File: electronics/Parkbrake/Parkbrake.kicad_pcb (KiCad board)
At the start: 2 copper layers, 101.6 x 114.3 mm, 353 parts, among them P1 Conn48pin, P2 JTAG, P3 UART, Q1 BSS138, Q10 IPD031N06L3 G, Q11 IPD031N06L3 G, Q12 NX3008CBKS, Q13 NX3008CBKS, Q14 IPD031N06L3 G, Q15 IPD031N06L3 G, Q16 IPD031N06L3 G, Q17 IPD031N06L3 G, Q18 NX3008CBKS, Q19 NX3008CBKS, Q2 BSS138, Q20 IPD031N06L3 G, Q21 IPD031N06L3 G, Q22 IPD031N06L3 G, Q23 IPD031N06L3 G, Q24 NX3008CBKS, Q25 NX3008CBKS, Q26 IPD031N06L3 G, Q27 IPD031N06L3 G, Q28 IPD031N06L3 G, Q29 IPD031N06L3 G, Q3 P-ch -40V 0.0035ohm, Q30 NX3008CBKS, Q31 BSS138, Q32 NTS4173, Q33 NX3008CBKS, Q4 P-ch -40V 0.0035ohm, Q5 BSS308, Q6 BSS308, Q7 NX3008CBKS, Q8 IPD031N06L3 G, Q9 IPD031N06L3 G, U1 74LVC00, U10 IRS2304, U11 ZXCT1082, U12 IRS2304, U13 LM2903, U14 IRS2304, U15 ZXCT1082, U16 IRS2304, U17 LM2903, U18 IRS2304, U19 ZXCT1082, U2 74LVC08, U20 IRS2304, U21 MIC2619, U22 MC34063, U23 LD1117S33CTR, U24 CAT25160_EEPROM, U25 STM32F373RBTx, U26 SN65HVD1050D, U27 SN74LVC245ADBR, U28 SN74HC20, U29 SN74HC02, U3 74LVC00, U30 SN74HC132, U31 MAX232, U32 MAX232, U33 NCV1124, U34 NCV1124, U35 74LVC08, U4 74LVC08, U5 LM2903, U6 IRS2304, U7 ZXCT1082, U8 IRS2304, U9 LM2903, Y1 24Mhz

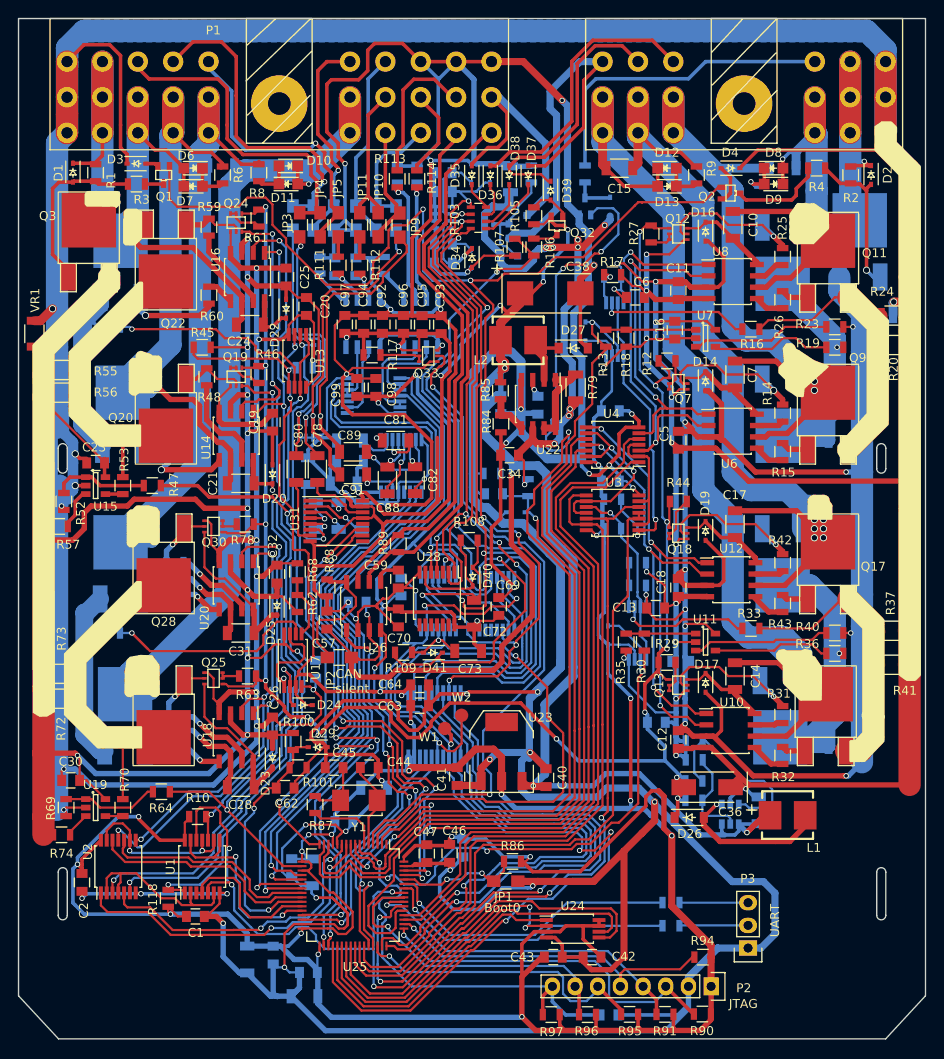
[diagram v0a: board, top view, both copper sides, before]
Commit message: Added copperareas
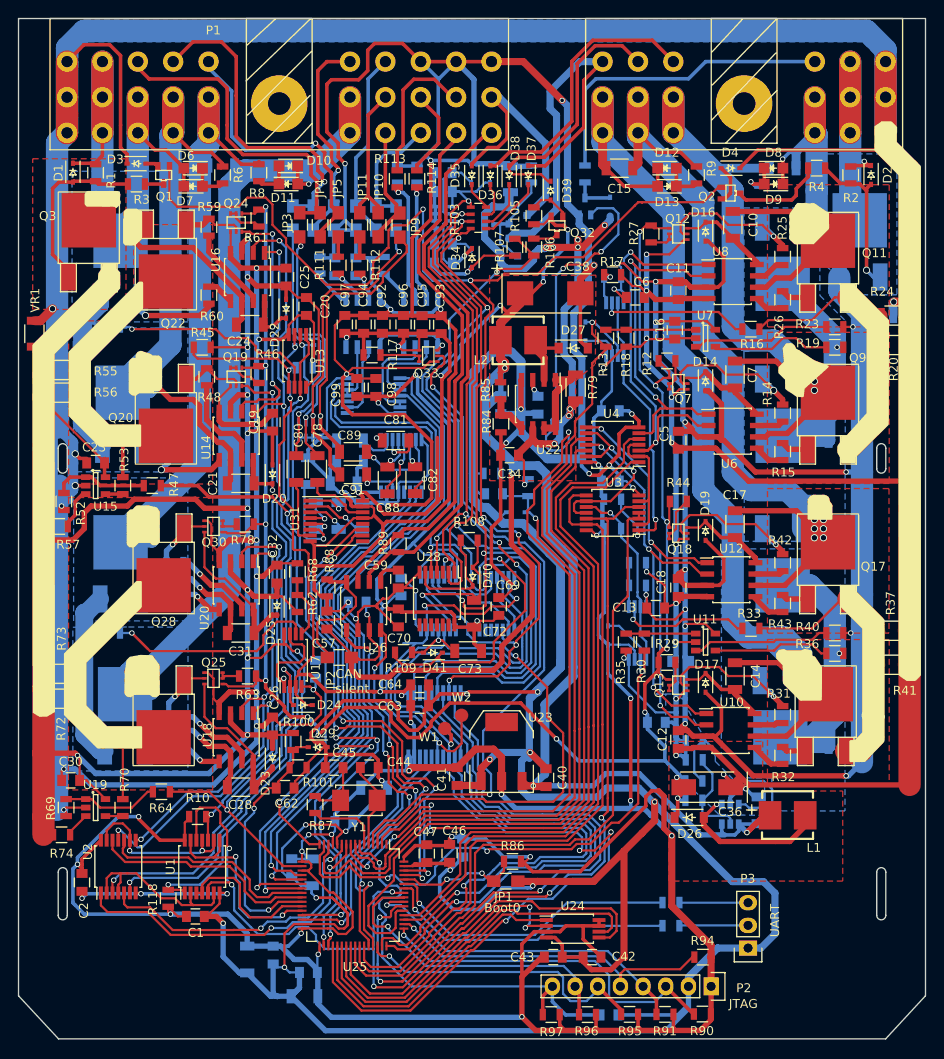
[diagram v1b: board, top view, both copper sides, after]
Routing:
- net GNDPWR: track 748.7 -> 754.2 mm, vias 30 -> 31
- added copper zone on F.Cu, net /+12V_BatF
- added copper zone on B.Cu, net /+12V_BatR
- added copper zone on F.Cu, net GNDPWR
- added copper zone on F.Cu, net LR_wheelsensor_in-
- added copper zone on B.Cu, net LeftFrontMotor+
- added copper zone on B.Cu, net LeftFrontMotor-
- added copper zone on F.Cu, net LeftRearMotor+
- added copper zone on F.Cu, net LeftRearMotor-
- added copper zone on B.Cu, net Net-(Q10-Pad2)
- added copper zone on B.Cu, net Net-(Q14-Pad2)
- added copper zone on F.Cu, net Net-(Q20-Pad2)
- added copper zone on F.Cu, net Net-(Q26-Pad2)
- added copper zone on B.Cu, net RightFrontMotor+
- added copper zone on B.Cu, net RightFrontMotor-
- added copper zone on F.Cu, net RightRearMotor+
- added copper zone on F.Cu, net RightRearMotor-
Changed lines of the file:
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@@
     (thickness 1.6)
     (drawings 87)
-    (tracks 6120)
+    (tracks 6125)
     (zones 0)
     (modules 353)
@@
     (34 B.Paste user)
     (35 F.Paste user)
-    (36 B.SilkS user hide)
+    (36 B.SilkS user)
     (37 F.SilkS user)
     (38 B.Mask user)
@@
   )
   (setup
-    (last_trace_width 1.2)
+    (last_trace_width 0.4)
     (user_trace_width 0.4)
     (user_trace_width 0.6)
@@
   (segment (start 131.15544 59.2099) (end 129.518 59.2099) (width 0.8) (layer B.Cu) (net 3))
   (segment (start 129.518 59.2099) (end 129.3749 59.0668) (width 0.8) (layer B.Cu) (net 3))
+  (segment (start 155.9306 126.1413) (end 155.9306 123.5202) (width 0.4) (layer B.Cu) (net 4))
+  (segment (start 155.9306 123.5202) (end 155.1813 122.7709) (width 0.4) (layer B.Cu) (net 4))
+  (via (at 155.1813 122.7709) (size 0.6) (drill 0.4) (layers F.Cu B.Cu) (net 4))
+  (segment (start 155.1813 122.7709) (end 155.96362 123.55322) (width 0.4) (layer F.Cu) (net 4))
+  (segment (start 155.96362 123.55322) (end 155.96362 124.206) (width 0.4) (layer F.Cu) (net 4))
   (segment (start 80.391 81.153) (end 80.391 84.3153) (width 1.2) (layer B.Cu) (net 4))
   (segment (start 80.391 84.3153) (end 80.6577 84.582) (width 1.2) (layer B.Cu) (net 4))
@@
     (connect_pads (clearance 0.508))
     (min_thickness 0.254)
-    (fill (arc_segments 16) (thermal_gap 0.508) (thermal_bridge_width 0.508))
+    (fill yes (arc_segments 16) (thermal_gap 0.508) (thermal_bridge_width 0.508))
     (polygon
       (pts
@@
     (connect_pads (clearance 0.508))
     (min_thickness 0.254)
-    (fill (arc_segments 16) (thermal_gap 0.508) (thermal_bridge_width 0.508))
+    (fill yes (arc_segments 16) (thermal_gap 0.508) (thermal_bridge_width 0.508))
     (polygon
       (pts
@@
       )
     )
+  )
+  (zone (net 17) (net_name LeftFrontMotor-) (layer B.Cu) (hatch edge 0.508)
+    (connect_pads yes (clearance 0.508))
+    (min_thickness 0.254)
+    (fill yes (arc_segments 16) (thermal_gap 0.508) (thermal_bridge_width 0.508))
+    (polygon
+      (pts
+        (xy 95.1738 55.1688) (xy 95.1738 72.0852) (xy 82.1944 72.0852) (xy 82.1944 55.2069) (xy 91.5924 55.2069)
+      )
+    )
+  )
+  (zone (net 15) (net_name LeftFrontMotor+) (layer B.Cu) (hatch edge 0.508)
+    (connect_pads yes (clearance 0.508))
+    (min_thickness 0.254)
+    (fill yes (arc_segments 16) (thermal_gap 0.508) (thermal_bridge_width 0.508))
+    (polygon
+      (pts
+        (xy 93.40215 72.771) (xy 95.1738 72.771) (xy 95.171024 72.78359) (xy 95.1865 72.7837) (xy 95.171003 72.783685)
+        (xy 95.1611 88.9) (xy 82.3595 88.8746) (xy 82.3341 72.771) (xy 91.6178 72.771) (xy 91.6178 72.7583)
+        (xy 93.40215 72.771)
+      )
+    )
+  )
+  (zone (net 21) (net_name RightFrontMotor-) (layer B.Cu) (hatch edge 0.508)
+    (connect_pads yes (clearance 0.508))
+    (min_thickness 0.254)
+    (fill yes (arc_segments 16) (thermal_gap 0.508) (thermal_bridge_width 0.508))
+    (polygon
+      (pts
+        (xy 95.1611 89.5604) (xy 95.1738 105.5751) (xy 82.3722 105.5878) (xy 82.3722 89.5731) (xy 82.3595 89.5604)
+      )
+    )
+  )
+  (zone (net 19) (net_name RightFrontMotor+) (layer B.Cu) (hatch edge 0.508)
+    (connect_pads yes (clearance 0.508))
+    (min_thickness 0.254)
+    (fill yes (arc_segments 16) (thermal_gap 0.508) (thermal_bridge_width 0.508))
+    (polygon
+      (pts
+        (xy 95.1865 106.2863) (xy 95.1738 122.3772) (xy 82.2833 122.3899) (xy 82.2833 106.2863) (xy 88.5063 106.2609)
+      )
+    )
+  )
+  (zone (net 197) (net_name /+12V_BatR) (layer B.Cu) (hatch edge 0.508)
+    (connect_pads yes (clearance 0.508))
+    (min_thickness 0.254)
+    (fill yes (arc_segments 16) (thermal_gap 0.508) (thermal_bridge_width 0.508))
+    (polygon
+      (pts
+        (xy 166.878 53.2638) (xy 174.5996 53.2638) (xy 174.5996 69.0499) (xy 170.4086 69.0499) (xy 166.5224 65.6971)
+        (xy 166.5224 53.2638) (xy 166.8399 53.2638)
+      )
+    )
+  )
+  (zone (net 101) (net_name "Net-(Q10-Pad2)") (layer B.Cu) (hatch edge 0.508)
+    (connect_pads yes (clearance 0.508))
+    (min_thickness 0.254)
+    (fill yes (arc_segments 16) (thermal_gap 0.508) (thermal_bridge_width 0.508))
+    (polygon
+      (pts
+        (xy 157.4673 59.3217) (xy 165.9763 59.3217) (xy 165.9636 69.1261) (xy 168.8338 71.9582) (xy 168.783 96.6597)
+        (xy 157.5054 96.6597) (xy 157.4673 75.7682) (xy 157.4673 64.5795)
+      )
+    )
+  )
+  (zone (net 214) (net_name "Net-(Q14-Pad2)") (layer B.Cu) (hatch edge 0.508)
+    (connect_pads yes (clearance 0.508))
+    (min_thickness 0.254)
+    (fill yes (arc_segments 16) (thermal_gap 0.508) (thermal_bridge_width 0.508))
+    (polygon
+      (pts
+        (xy 168.783 97.536) (xy 168.783 126.873) (xy 160.5788 126.8603) (xy 160.5788 123.2027) (xy 157.099 123.1392)
+        (xy 154.9273 120.9421) (xy 154.9527 97.5106) (xy 168.783 97.5106) (xy 168.783 97.536)
+      )
+    )
+  )
+  (zone (net 8) (net_name LeftRearMotor-) (layer F.Cu) (hatch edge 0.508)
+    (connect_pads yes (clearance 0.508))
+    (min_thickness 0.254)
+    (fill yes (arc_segments 16) (thermal_gap 0.508) (thermal_bridge_width 0.508))
+    (polygon
+      (pts
+        (xy 160.0962 56.7182) (xy 173.736 56.7182) (xy 173.736 72.644) (xy 160.0962 72.644) (xy 160.0962 57.3405)
+      )
+    )
+  )
+  (zone (net 6) (net_name LeftRearMotor+) (layer F.Cu) (hatch edge 0.508)
+    (connect_pads yes (clearance 0.508))
+    (min_thickness 0.254)
+    (fill yes (arc_segments 16) (thermal_gap 0.508) (thermal_bridge_width 0.508))
+    (polygon
+      (pts
+        (xy 160.0835 73.2536) (xy 173.736 73.2536) (xy 173.736 90.1827) (xy 160.0962 90.1827) (xy 160.0962 83.7438)
+      )
+    )
+  )
+  (zone (net 12) (net_name RightRearMotor-) (layer F.Cu) (hatch edge 0.508)
+    (connect_pads yes (clearance 0.508))
+    (min_thickness 0.254)
+    (fill yes (arc_segments 16) (thermal_gap 0.508) (thermal_bridge_width 0.508))
+    (polygon
+      (pts
+        (xy 160.0962 90.7542) (xy 173.7106 90.7542) (xy 173.7106 106.9467) (xy 160.0962 106.9467) (xy 160.0962 100.3173)
+      )
+    )
+  )
+  (zone (net 10) (net_name RightRearMotor+) (layer F.Cu) (hatch edge 0.508)
+    (connect_pads yes (clearance 0.508))
+    (min_thickness 0.254)
+    (fill yes (arc_segments 16) (thermal_gap 0.508) (thermal_bridge_width 0.508))
+    (polygon
+      (pts
+        (xy 160.0962 107.6706) (xy 173.736 107.6706) (xy 173.736 123.8758) (xy 160.0962 123.8758) (xy 160.0962 111.1377)
+      )
+    )
+  )
+  (zone (net 196) (net_name /+12V_BatF) (layer F.Cu) (hatch edge 0.508)
+    (connect_pads yes (clearance 0.508))
+    (min_thickness 0.254)
+    (fill yes (arc_segments 16) (thermal_gap 0.508) (thermal_bridge_width 0.508))
+    (polygon
+      (pts
+        (xy 77.7875 53.8099) (xy 88.2396 53.8099) (xy 88.2396 70.6882) (xy 77.7875 70.6882) (xy 77.7875 57.5056)
+      )
+    )
+  )
+  (zone (net 218) (net_name "Net-(Q20-Pad2)") (layer F.Cu) (hatch edge 0.508)
+    (connect_pads yes (clearance 0.508))
+    (min_thickness 0.254)
+    (fill yes (arc_segments 16) (thermal_gap 0.508) (thermal_bridge_width 0.508))
+    (polygon
+      (pts
+        (xy 97.9551 90.2462) (xy 81.8134 90.2462) (xy 81.8134 71.9709) (xy 88.1126 71.9709) (xy 89.1286 71.0946)
+        (xy 89.0778 61.1886) (xy 97.9551 61.1886) (xy 97.9551 90.2462)
+      )
+    )
+  )
+  (zone (net 218) (net_name "Net-(Q20-Pad2)") (layer F.Cu) (hatch edge 0.508)
+    (connect_pads yes (clearance 0.508))
+    (min_thickness 0.254)
+    (fill yes (arc_segments 16) (thermal_gap 0.508) (thermal_bridge_width 0.508))
+    (polygon
+      (pts
+        (xy 97.9678 61.1886) (xy 97.9678 61.2013) (xy 97.9551 61.1886) (xy 97.9678 61.1886)
+      )
+    )
+  )
+  (zone (net 222) (net_name "Net-(Q26-Pad2)") (layer F.Cu) (hatch edge 0.508)
+    (connect_pads yes (clearance 0.508))
+    (min_thickness 0.254)
+    (fill yes (arc_segments 16) (thermal_gap 0.508) (thermal_bridge_width 0.508))
+    (polygon
+      (pts
+        (xy 97.9551 91.7575) (xy 97.9551 124.5108) (xy 81.788 124.5108) (xy 81.788 113.9698) (xy 81.813328 91.7575)
+        (xy 97.9551 91.7575)
+      )
+    )
+  )
+  (zone (net 222) (net_name "Net-(Q26-Pad2)") (layer F.Cu) (hatch edge 0.508)
+    (connect_pads yes (clearance 0.508))
+    (min_thickness 0.254)
+    (fill yes (arc_segments 16) (thermal_gap 0.508) (thermal_bridge_width 0.508))
+    (polygon
+      (pts
+        (xy 81.7499 91.7575) (xy 81.8134 91.694) (xy 81.813328 91.7575) (xy 81.7499 91.7575)
+      )
+    )
+  )
+  (zone (net 2) (net_name LR_wheelsensor_in-) (layer F.Cu) (hatch edge 0.508)
+    (connect_pads (clearance 0.508))
+    (min_thickness 0.254)
+    (fill yes (arc_segments 16) (thermal_gap 0.508) (thermal_bridge_width 0.508))
+    (polygon
+      (pts
+        (xy 128.9812 76.7334) (xy 128.9812 89.8779) (xy 138.6332 89.8779) (xy 138.6078 78.6638) (xy 140.8176 76.8096)
+        (xy 140.8811 66.8528) (xy 128.9685 66.8909) (xy 128.9685 67.1703)
+      )
+    )
+  )
+  (zone (net 4) (net_name GNDPWR) (layer F.Cu) (hatch edge 0.508)
+    (connect_pads (clearance 0.508))
+    (min_thickness 0.254)
+    (fill yes (arc_segments 16) (thermal_gap 0.508) (thermal_bridge_width 0.508))
+    (polygon
+      (pts
+        (xy 149.0599 119.0752) (xy 159.5628 119.0752) (xy 159.5628 124.6378) (xy 168.529 124.6378) (xy 168.529 134.7216)
+        (xy 149.0472 134.7216) (xy 149.0472 132.0927)
+      )
+    )
+  )
+  (zone (net 4) (net_name GNDPWR) (layer B.Cu) (hatch edge 0.508)
+    (connect_pads (clearance 0.508))
+    (min_thickness 0.254)
+    (fill yes (arc_segments 16) (thermal_gap 0.508) (thermal_bridge_width 0.508))
+    (polygon
+      (pts
+        (xy 147.6121 113.7666) (xy 150.1394 113.7666) (xy 154.2542 120.7262) (xy 154.2542 121.3231) (xy 156.8831 123.952)
+        (xy 159.7787 123.952) (xy 159.7787 127.381) (xy 154.6606 127.2667) (xy 148.6916 121.5263) (xy 148.7043 113.792)
+        (xy 148.1074 113.792)
+      )
+    )

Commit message: Changed solder trace zones, was silkscreen now soldermask
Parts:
- added REF**: Symbol_OSHW-Logo_SilkScreen, Symbols:Symbol_OSHW-Logo_SilkScreen, F.Cu at (86.1, 142.1)
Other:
- board text added: "github.com/mumme74/CarTransporter"

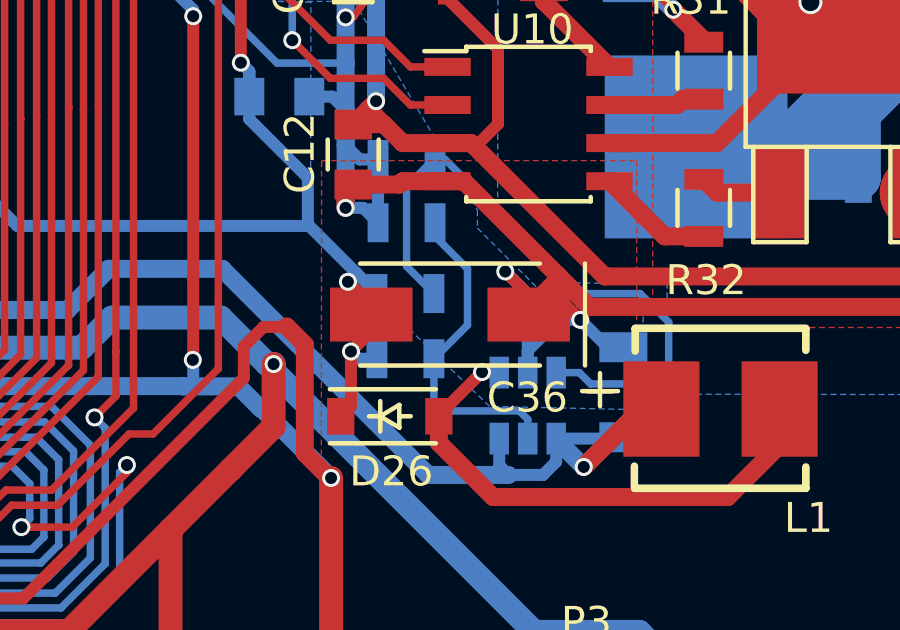
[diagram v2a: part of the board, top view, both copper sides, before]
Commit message: minor tweaks to pcb, had a cap on wrong polarity
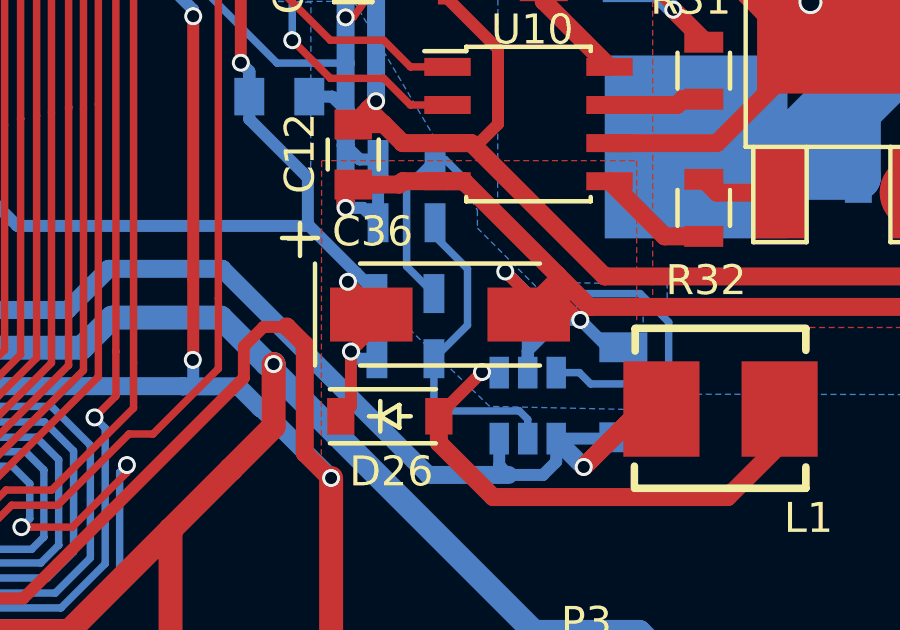
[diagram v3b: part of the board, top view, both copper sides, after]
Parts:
- turned C36 to 0 degrees
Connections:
- C36 pad 1: GNDPWR -> gate_drive_24V
- C36 pad 2: gate_drive_24V -> GNDPWR

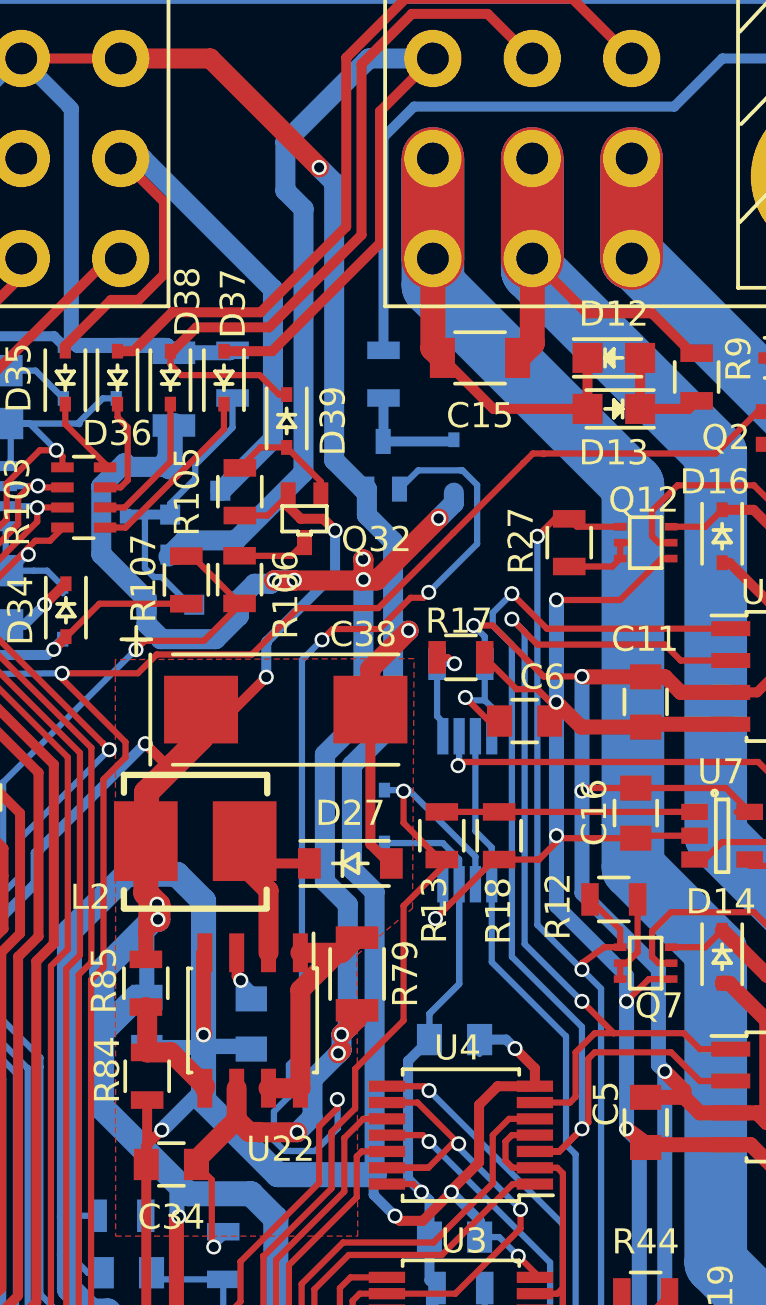
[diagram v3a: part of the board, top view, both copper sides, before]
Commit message: reduce switching noise from 5v regulator circuit
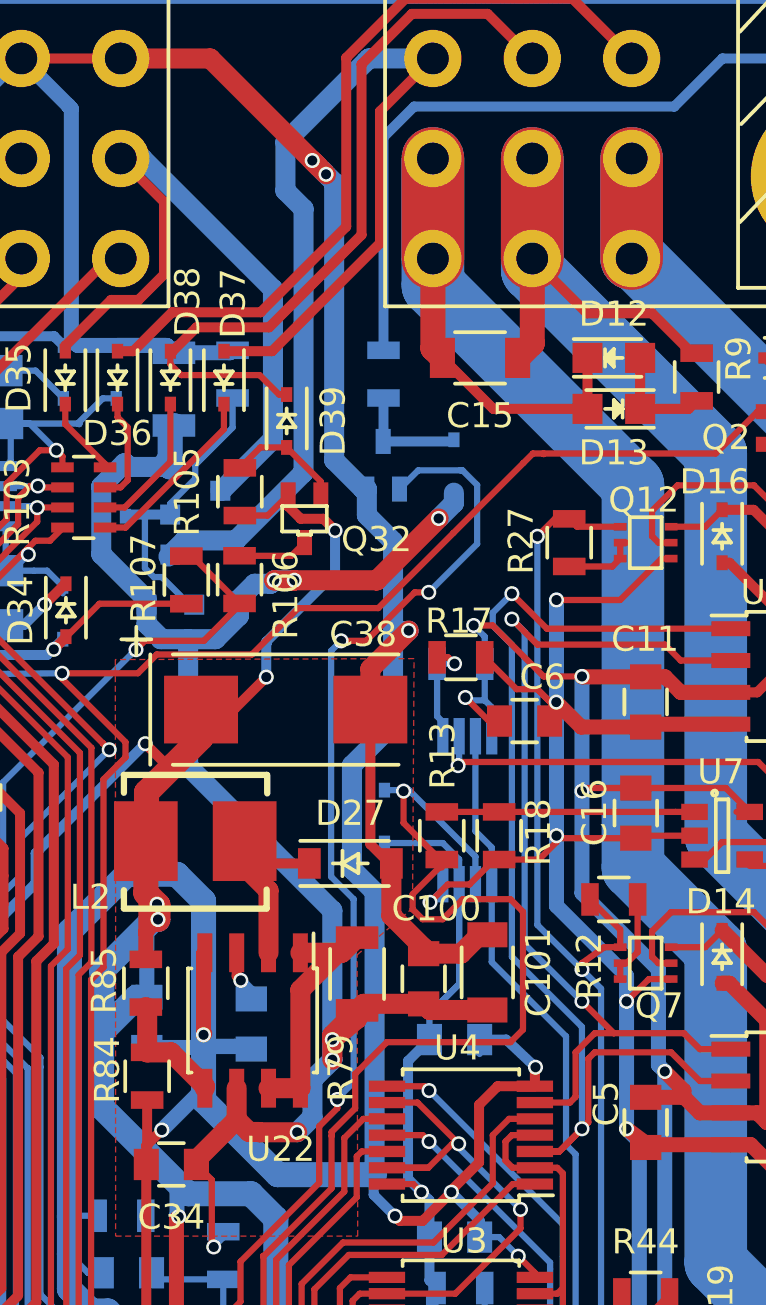
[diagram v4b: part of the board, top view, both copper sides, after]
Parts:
- added C100: 10u, myfootprints:CP_0805, F.Cu at (141.3, 79.6)
- added C101: 1u, Capacitors_SMD:C_1206, F.Cu at (143.8, 79.4)
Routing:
- net LeftRear_CS: track 102.0 -> 112.0 mm
- net LR_wheelsensor_in-: track 964.7 -> 972.9 mm, vias 37 -> 38
- net INDICATOR_ON: track 113.0 -> 106.4 mm
- net +12V_Feed: track 65.1 -> 70.7 mm, vias 9 -> 7
